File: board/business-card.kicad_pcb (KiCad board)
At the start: 2 copper layers, 88.9 x 50.8 mm, 40 parts, among them SW1 PTS_540, U1 STM8S003F3U, U2 KX003-1077

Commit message: layout leds, add cam to ignore
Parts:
- moved D15 83.9 mm to (155.5, 96.1)
- moved D2 81.9 mm to (145.4, 95.0)
- moved D14 78.1 mm to (155.5, 102.7)
- moved D7 78.1 mm to (145.4, 88.8)
- moved D4 76.0 mm to (142.8, 103.0)
- moved D8 75.7 mm to (139.2, 90.8)
- moved D13 71.2 mm to (151.6, 108.0)
- moved D1 69.3 mm to (145.4, 99.4)
- moved D6 69.1 mm to (149.6, 98.0)
- moved D12 68.2 mm to (145.4, 110.0)
- moved D5 65.9 mm to (148.0, 103.0)
- moved D10 64.6 mm to (135.3, 102.7)
- moved D11 64.5 mm to (139.2, 108.0)
- moved R10 64.4 mm to (122.8, 32.1)
- moved R12 64.4 mm to (103.6, 45.7)
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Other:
- outline, holes or cut-outs redrawn
- board text added: "Colin Holzman Embedded Systems Engineer"

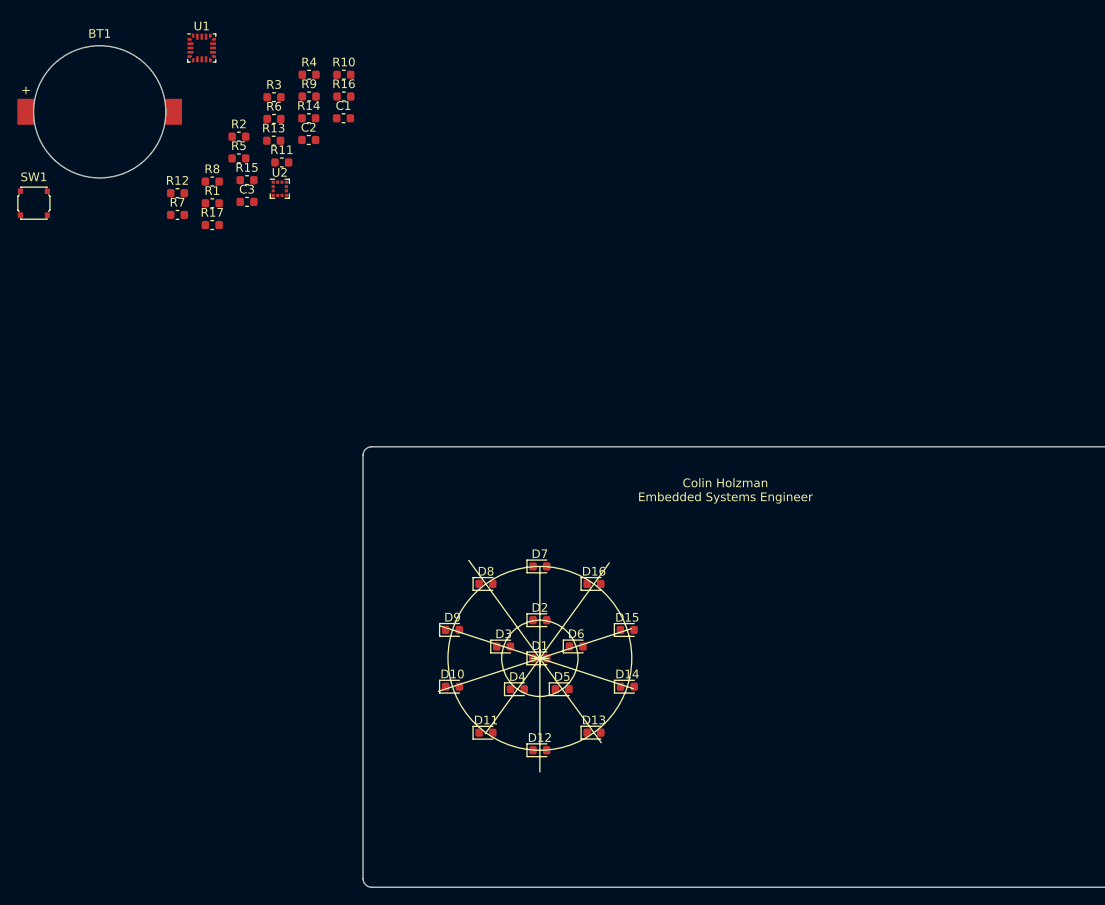
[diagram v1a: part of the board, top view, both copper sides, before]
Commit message: rotate leds and arrange resistors
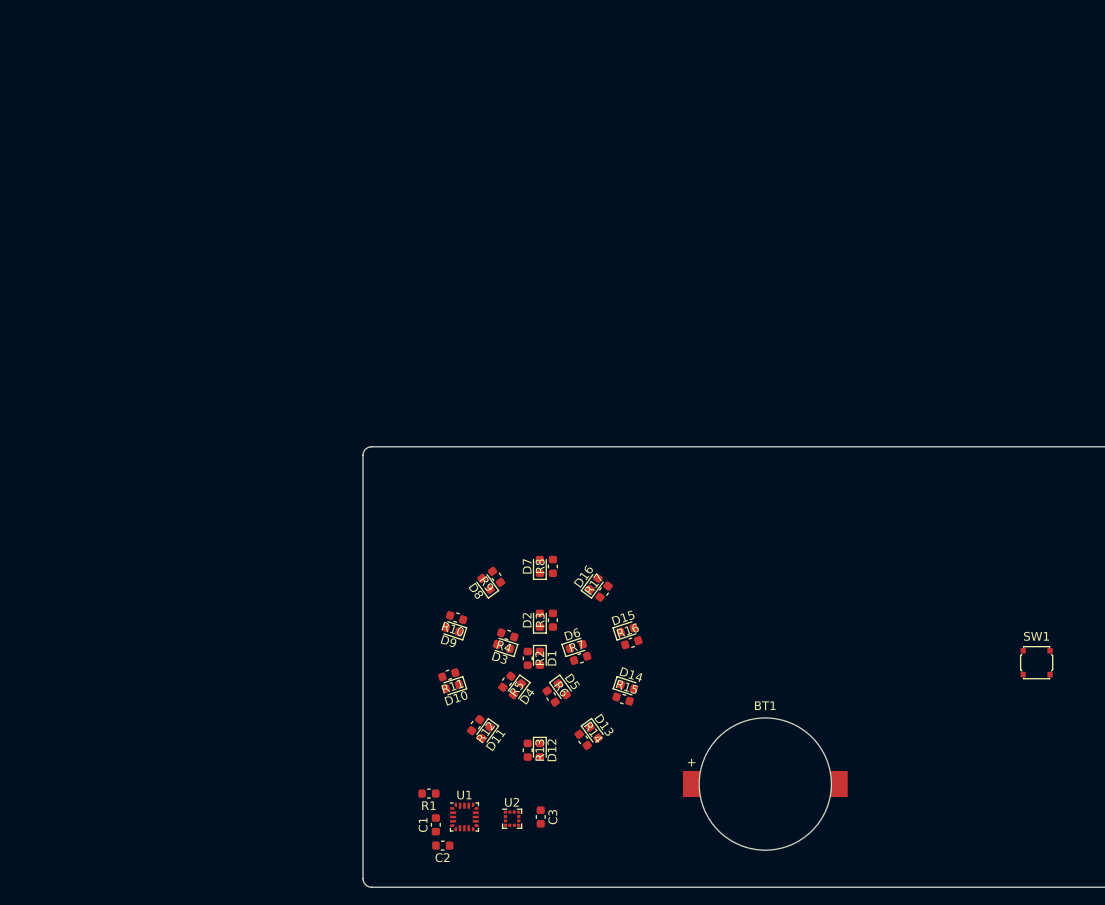
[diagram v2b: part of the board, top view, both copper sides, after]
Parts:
- moved SW1 127.2 mm to (202.7, 99.9)
- moved BT1 109.1 mm to (171.4, 113.9)
- moved U1 93.7 mm to (136.7, 117.7)
- moved C2 82.8 mm to (134.2, 121.0), turned to 180 degrees
- moved C1 82.2 mm to (133.4, 118.6), turned to 90 degrees
- moved C3 78.6 mm to (145.5, 117.7), turned to 270 degrees
- moved R14 78.4 mm to (150.4, 108.8), turned to 306 degrees
- moved U2 77.4 mm to (142.2, 117.9)
- moved R13 76.2 mm to (144.0, 110.0), turned to 270 degrees
- moved R15 73.9 mm to (155.0, 104.1), turned to 342 degrees
- moved R6 73.9 mm to (146.7, 103.8), turned to 306 degrees
- moved R1 72.5 mm to (132.6, 115.0), turned to 180 degrees
- moved R16 71.2 mm to (156.0, 97.6), turned to 18 degrees
- moved R12 70.3 mm to (138.0, 107.1), turned to 234 degrees
- moved R7 69.1 mm to (150.1, 99.4), turned to 18 degrees
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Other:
- board text removed: "Colin Holzman Embedded Systems Engineer"

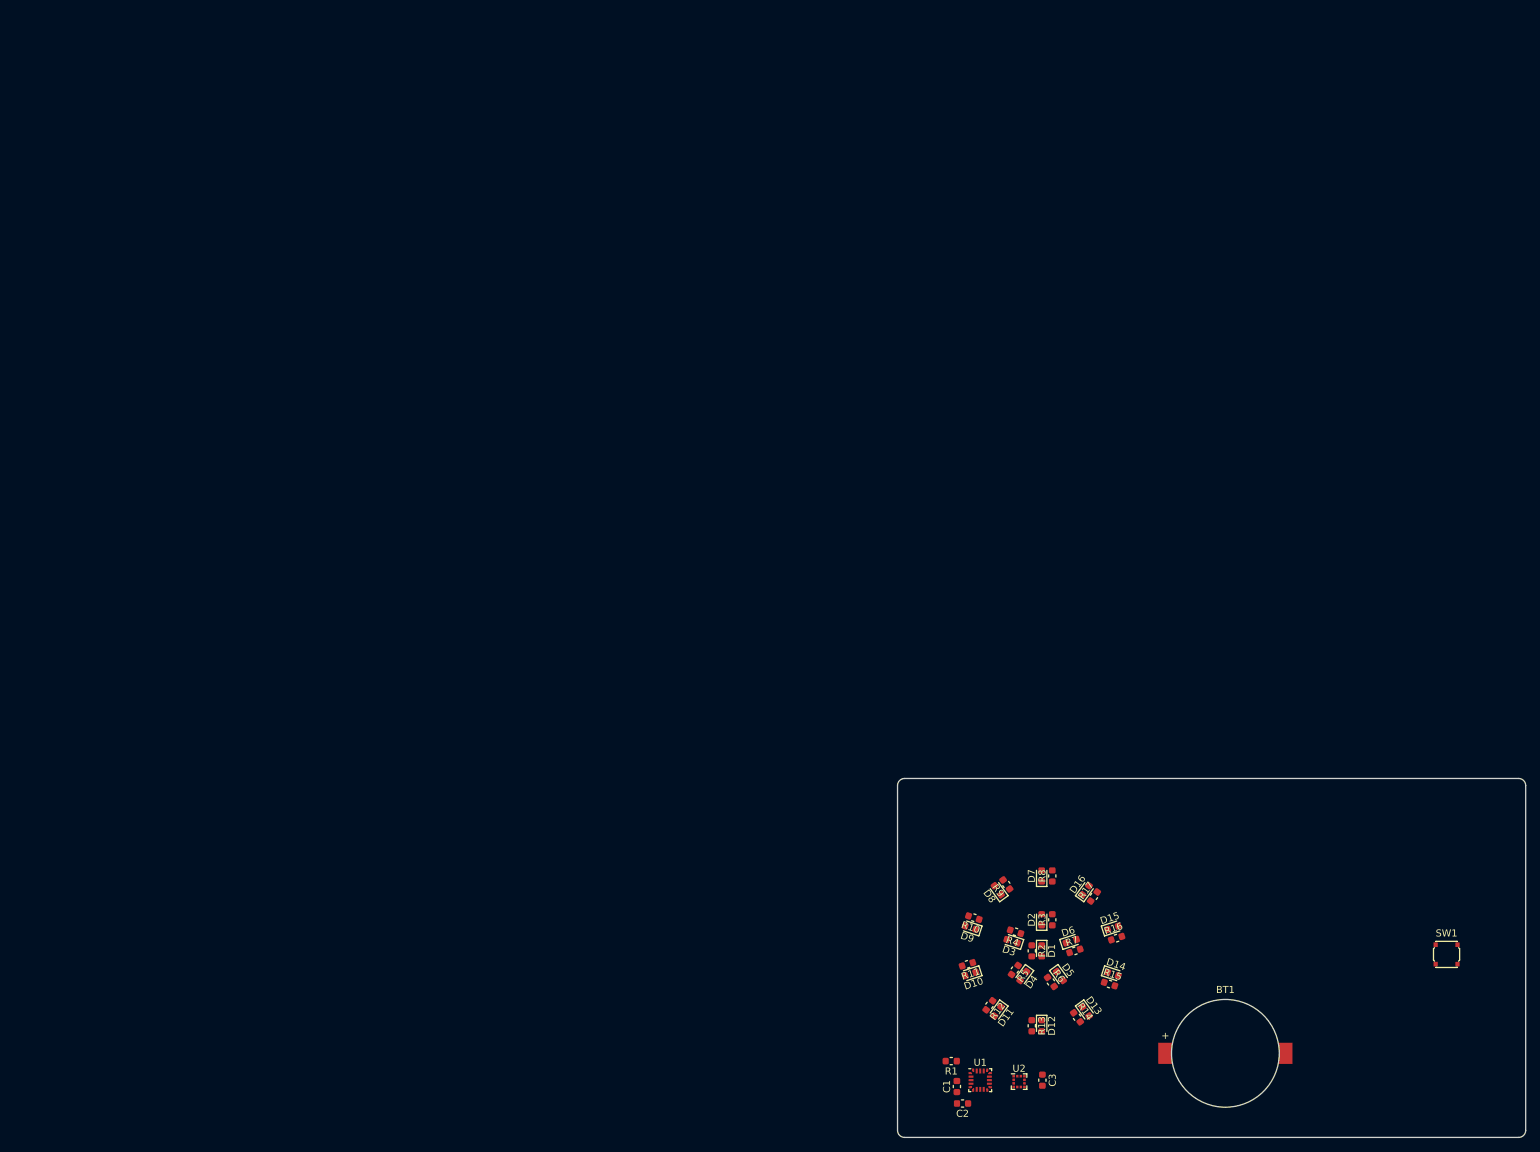
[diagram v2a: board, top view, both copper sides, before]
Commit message: Annotated board, added some part numbers and footprints.
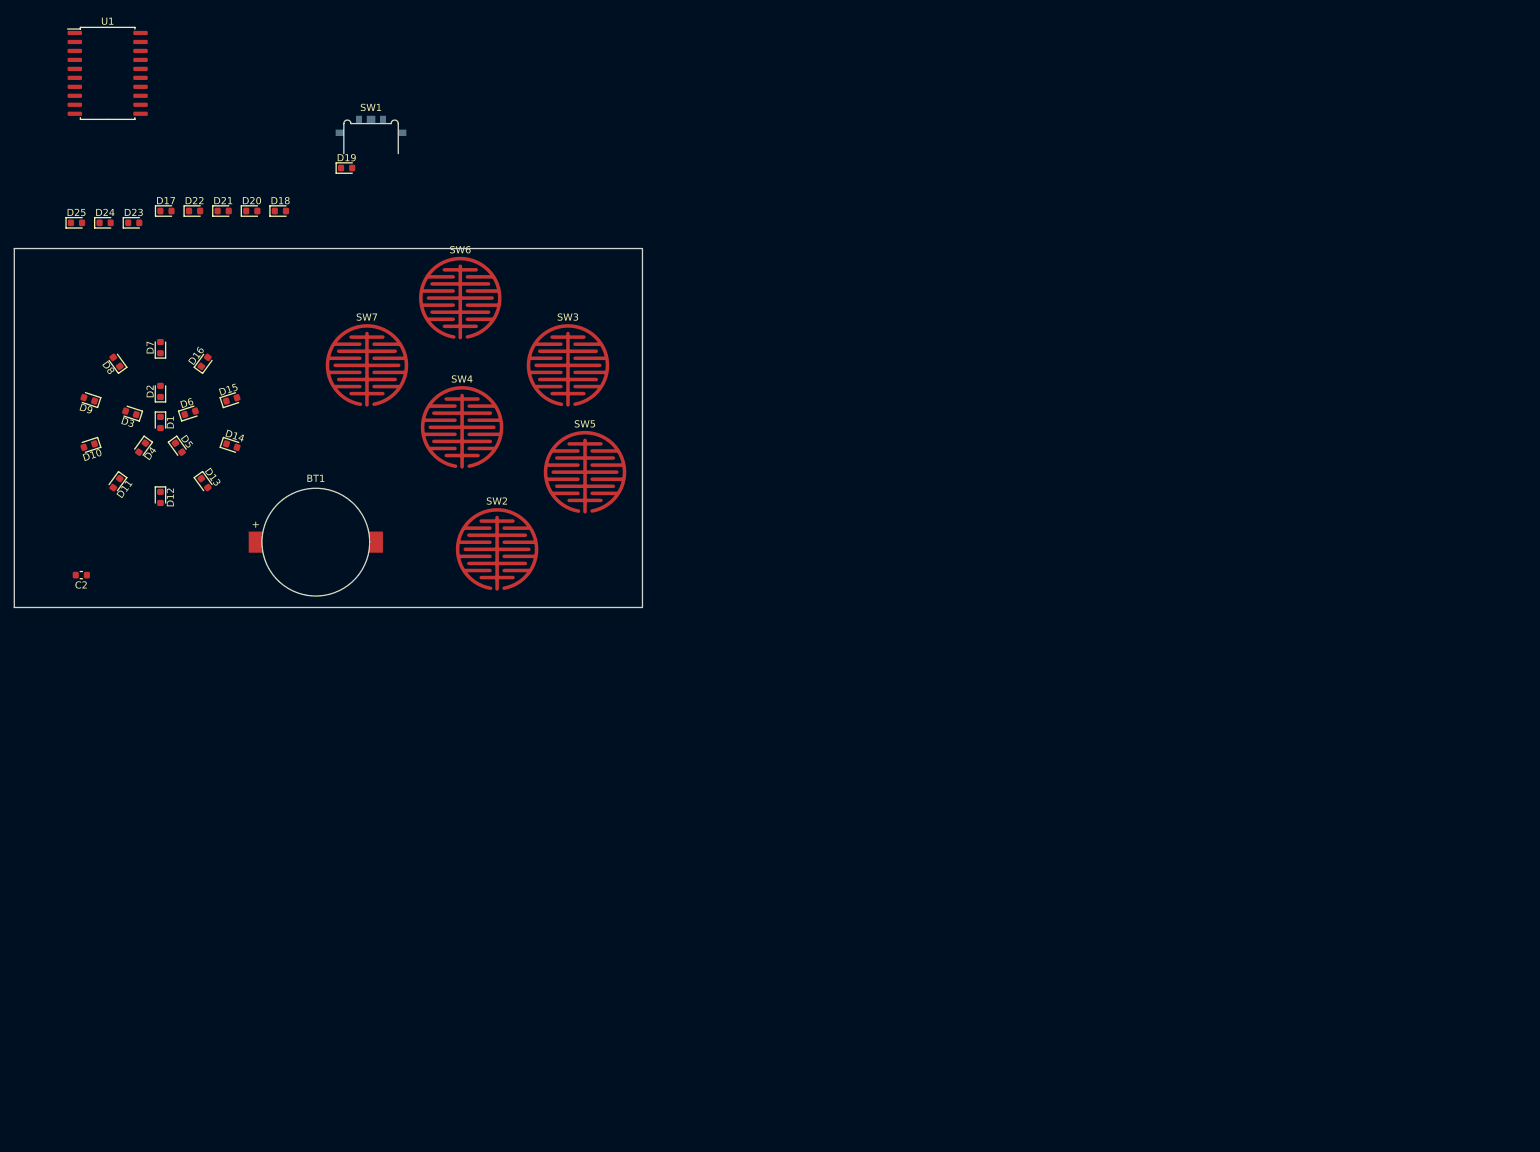
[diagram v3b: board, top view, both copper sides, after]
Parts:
- removed C1, C3: 0.1 uF, Capacitor_SMD:C_0603_1608Metric
- removed R1: 10 K, Resistor_SMD:R_0603_1608Metric
- removed R10, R11, R12, R13, R14, R15, R16, R17, R2, R3, R4, R5, R6, R7, R8, R9: 600, Resistor_SMD:R_0603_1608Metric
- removed U2: KX003-1077, Package_LGA:LGA-12_2x2mm_P0.5mm
- added D17: LED, LED_SMD:LED_0603_1608Metric, F.Cu at (21.5, -5.31)
- added D18: LED, LED_SMD:LED_0603_1608Metric, F.Cu at (37.7, -5.31)
- added D19: LED, LED_SMD:LED_0603_1608Metric, F.Cu at (47.0, -11.4)
- added D20: LED, LED_SMD:LED_0603_1608Metric, F.Cu at (33.6, -5.31)
- added D21: LED, LED_SMD:LED_0603_1608Metric, F.Cu at (29.6, -5.31)
- added D22: LED, LED_SMD:LED_0603_1608Metric, F.Cu at (25.5, -5.31)
- added D23: LED, LED_SMD:LED_0603_1608Metric, F.Cu at (16.9, -3.64)
- added D24: LED, LED_SMD:LED_0603_1608Metric, F.Cu at (12.9, -3.64)
- added D25: LED, LED_SMD:LED_0603_1608Metric, F.Cu at (8.80, -3.64)
- added SW2: Mutual_Capacitance_Button, colinholzman:Mutual_Capacitance_Button, F.Cu at (68.3, 42.6)
- added SW3: Mutual_Capacitance_Button, colinholzman:Mutual_Capacitance_Button, F.Cu at (78.4, 16.5)
- added SW4: Mutual_Capacitance_Button, colinholzman:Mutual_Capacitance_Button, F.Cu at (63.4, 25.3)
- added SW5: Mutual_Capacitance_Button, colinholzman:Mutual_Capacitance_Button, F.Cu at (80.8, 31.6)
- added SW6: Mutual_Capacitance_Button, colinholzman:Mutual_Capacitance_Button, F.Cu at (63.1, 7.01)
- added SW7: Mutual_Capacitance_Button, colinholzman:Mutual_Capacitance_Button, F.Cu at (49.9, 16.5)
- SW1: value PTS_540 -> SW_SPDT; footprint C_K:PTS_540 -> colinholzman:JSX08001SAQNL-through-board-mount
- U1: value STM8S003F3U -> ATtiny1616-S; footprint Package_DFN_QFN:ST_UFQFPN-20_3x3mm_P0.5mm -> Package_SO:SOIC-20W_7.5x12.8mm_P1.27mm
- moved SW1 189.8 mm to (50.5, -13.4)
- moved U1 188.6 mm to (13.2, -24.8)
- moved BT1 147.7 mm to (42.7, 41.6)
- moved D1 145.4 mm to (20.7, 24.6)
- moved D10 145.4 mm to (10.6, 27.9)
- moved D12 145.4 mm to (20.7, 35.2)
- moved D2 145.4 mm to (20.7, 20.2)
- moved D3 145.4 mm to (16.5, 23.3)
- moved D6 145.4 mm to (24.9, 23.3)
- moved D9 145.4 mm to (10.6, 21.3)
- moved C2 145.4 mm to (9.49, 46.2)
- moved D11 145.4 mm to (14.5, 33.2)
- moved D13 145.4 mm to (26.9, 33.2)
- moved D14 145.4 mm to (30.8, 27.9)
- moved D15 145.4 mm to (30.8, 21.4)
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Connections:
- D1 pad 2: Net-(D1-Pad2) -> /COL0
- D10 pad 2: Net-(D10-Pad2) -> /COL0
- D11 pad 2: Net-(D11-Pad2) -> /COL1
- D12 pad 2: Net-(D12-Pad2) -> /COL1
- D13 pad 2: Net-(D13-Pad2) -> /COL2
- D14 pad 2: Net-(D14-Pad2) -> /COL2
- D15 pad 2: Net-(D15-Pad2) -> /COL3
- D16 pad 2: Net-(D16-Pad2) -> /COL3
- D2 pad 2: Net-(D2-Pad2) -> /COL0
- D3 pad 2: Net-(D3-Pad2) -> /COL1
- D4 pad 2: Net-(D4-Pad2) -> /COL1
- D5 pad 2: Net-(D5-Pad2) -> /COL2
- D6 pad 2: Net-(D6-Pad2) -> /COL2
- D7 pad 2: Net-(D7-Pad2) -> /COL3
- D8 pad 2: Net-(D8-Pad2) -> /COL3
- D9 pad 2: Net-(D9-Pad2) -> /COL0
- SW1 pad 1: Net-(BT1-Pad1) -> (no net)
- U1 pad 1: /NRESET -> /VDD
- U1 pad 10: /ROW0 -> (no net)
- U1 pad 11: /ROW1 -> (no net)
- U1 pad 12: /ROW2 -> (no net)
- U1 pad 13: /ROW3 -> (no net)
- U1 pad 14: Net-(U1-Pad14) -> (no net)
- U1 pad 15: /SWIM -> (no net)
- U1 pad 16: /COL0 -> (no net)
- U1 pad 17: /COL1 -> (no net)
- U1 pad 18: /COL2 -> (no net)
- U1 pad 19: /COL3 -> (no net)
- U1 pad 2: Net-(U1-Pad2) -> (no net)
- U1 pad 20: Net-(U1-Pad20) -> /GND
- U1 pad 3: Net-(U1-Pad3) -> (no net)
- U1 pad 4: /GND -> (no net)
- U1 pad 5: Net-(C1-Pad1) -> (no net)
- U1 pad 6: /VDD -> (no net)
- U1 pad 7: Net-(U1-Pad7) -> (no net)
- U1 pad 8: /SDA -> (no net)
- U1 pad 9: /SCL -> (no net)
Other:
- outline, holes or cut-outs redrawn

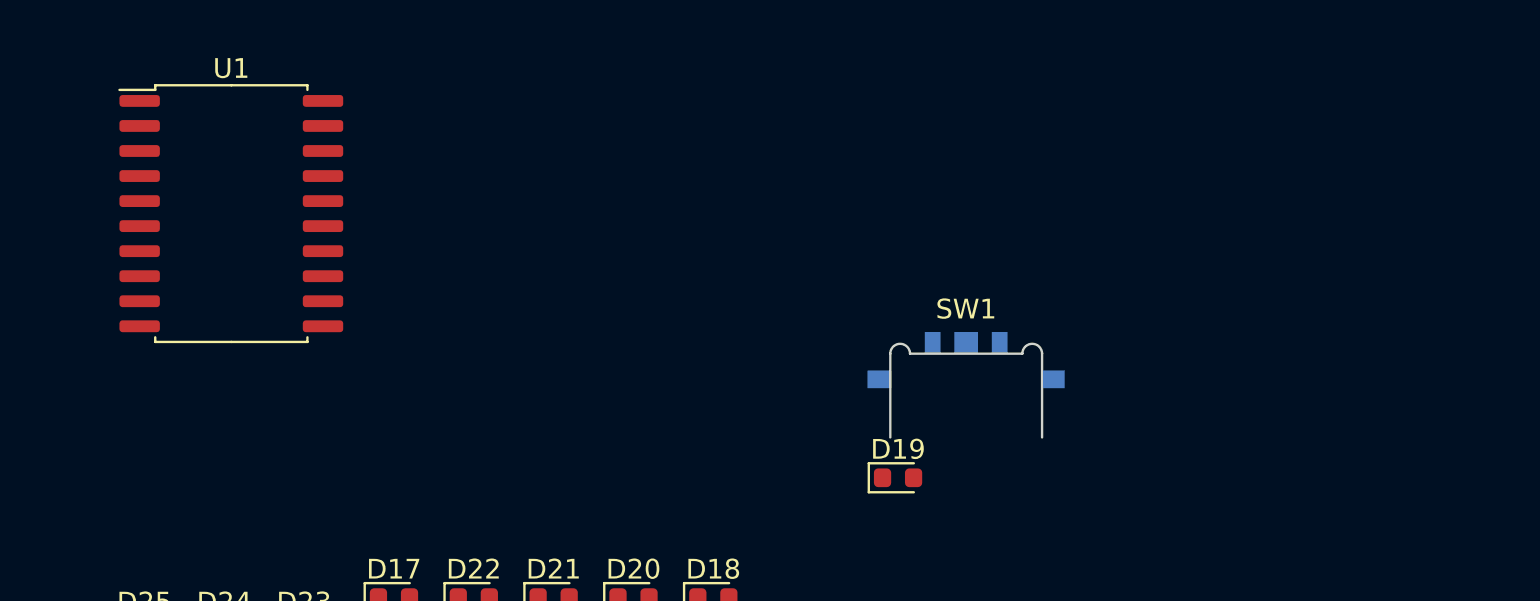
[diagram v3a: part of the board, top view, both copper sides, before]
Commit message: Updated footprints for mcu and switch.
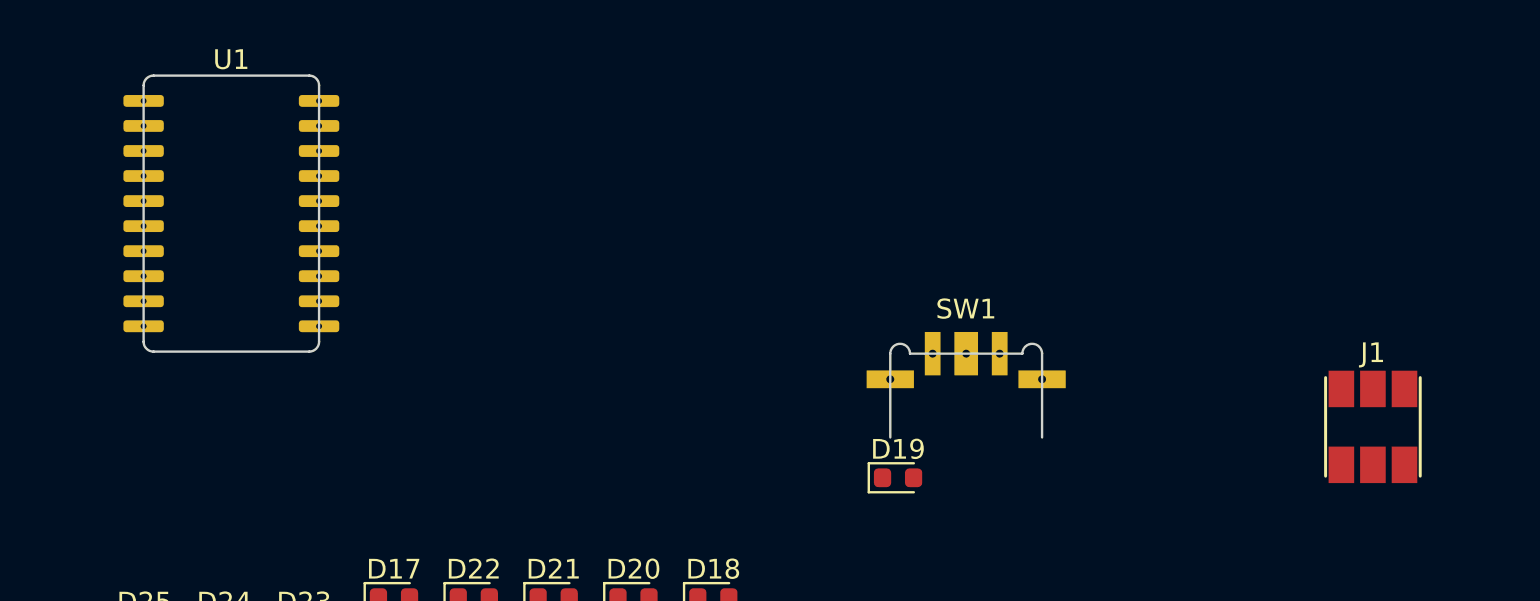
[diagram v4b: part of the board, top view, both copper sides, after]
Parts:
- added J1: Conn_01x06, colinholzman:Molex_788641001_mating_pad_layout, F.Cu at (71.1, -14.0)
- SW1: footprint colinholzman:JSX08001SAQNL-through-board-mount -> colinholzman:JSX08001SAQNL_through_board_mount
- U1: footprint Package_SO:SOIC-20W_7.5x12.8mm_P1.27mm -> colinholzman:SOIC-20W_7.5x12.8mm_P1.27mm_through_board_mount
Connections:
- U1 pad 16: (no net) -> /UPDI_DATA
